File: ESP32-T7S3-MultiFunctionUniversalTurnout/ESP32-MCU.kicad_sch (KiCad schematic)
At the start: 7 parts, among them U201 TTGO-T7_S3-V1.1

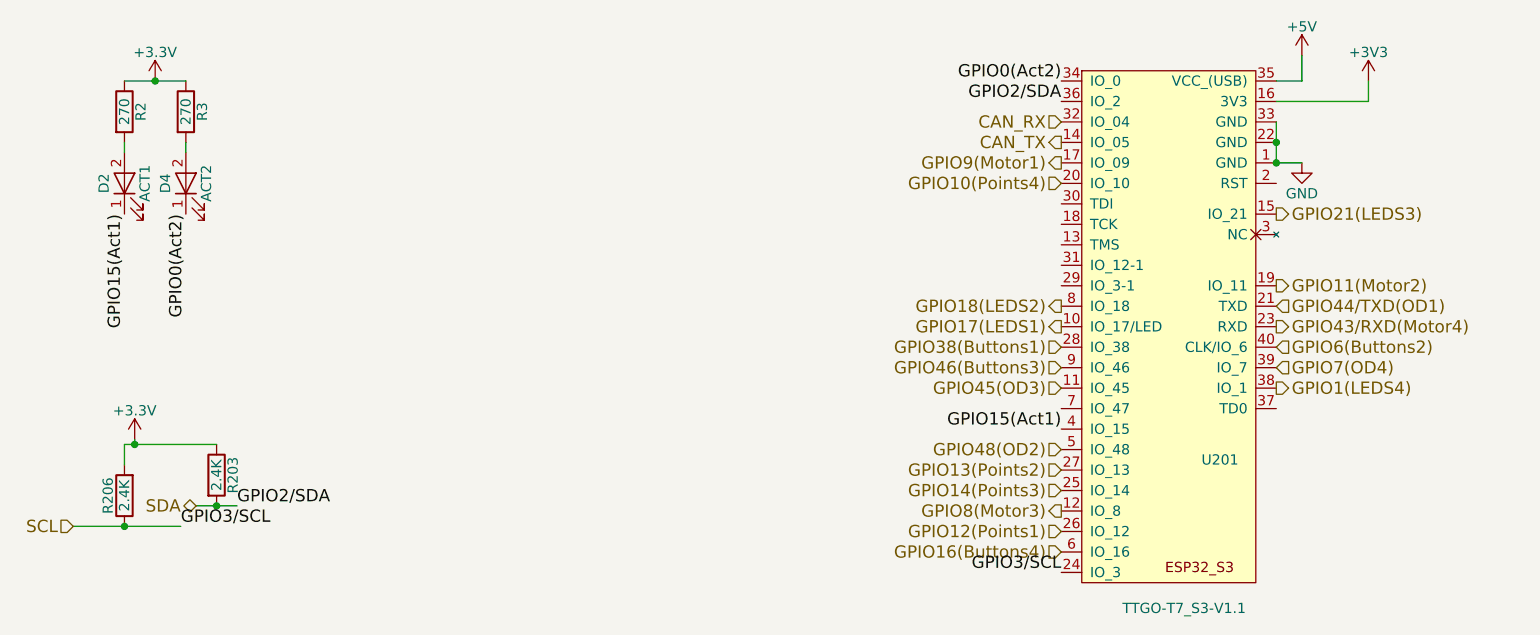
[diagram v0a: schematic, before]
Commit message: Change SDA from IO2 to IO40.
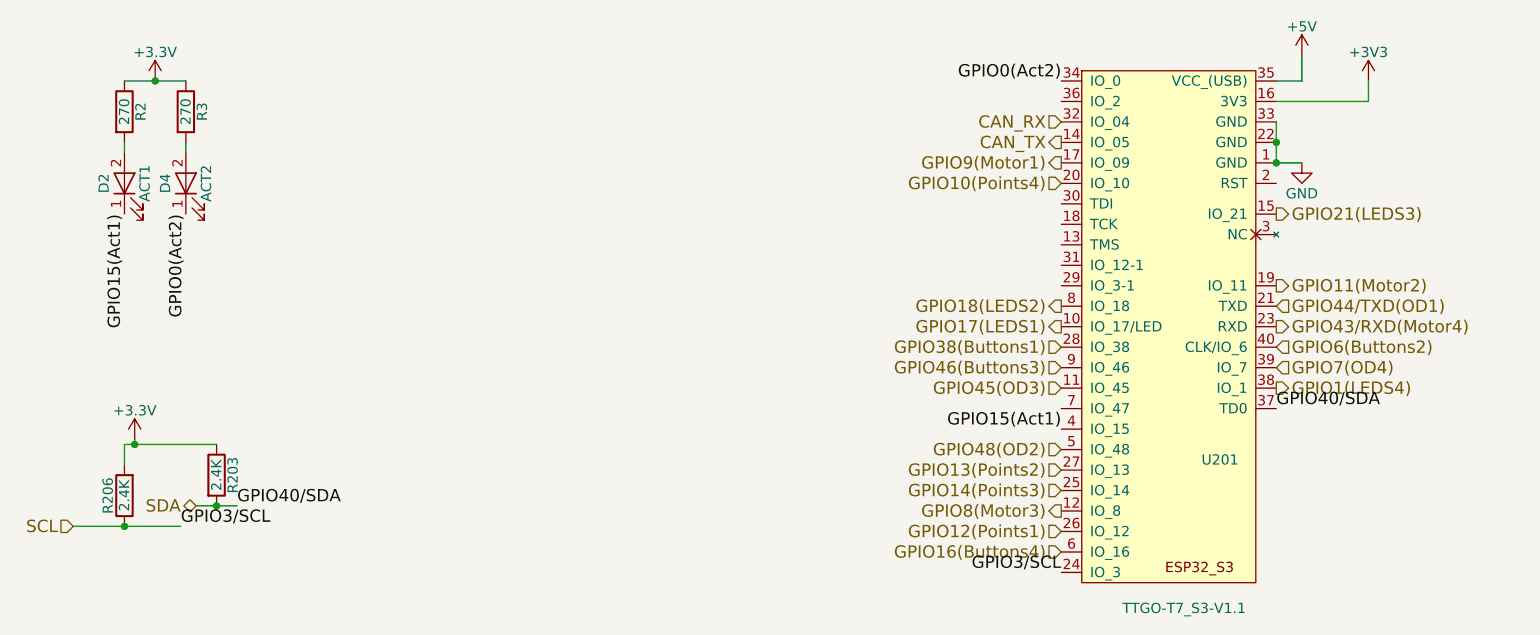
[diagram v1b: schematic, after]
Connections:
- net SDA: now also U201.37 (TD0); no longer U201.36 (IO_2)
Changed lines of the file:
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@@
     (effects (font (size 1.524 1.524)) (justify right bottom))
   )
-  (label "GPIO2/SDA" (at 213.995 66.04 180)
-    (effects (font (size 1.524 1.524)) (justify right bottom))
+  (label "GPIO40{slash}SDA" (at 240.665 104.14 0)
+    (effects (font (size 1.524 1.524)) (justify left bottom))
   )
   (label "GPIO3/SCL" (at 104.775 118.745 0)
@@
     (effects (font (size 1.524 1.524)) (justify right bottom))
   )
-  (label "GPIO2/SDA" (at 111.76 116.205 0)
+  (label "GPIO40{slash}SDA" (at 111.76 116.205 0)
     (effects (font (size 1.524 1.524)) (justify left bottom))
   )

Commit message: Reroute GPIOs using UART0 lines.
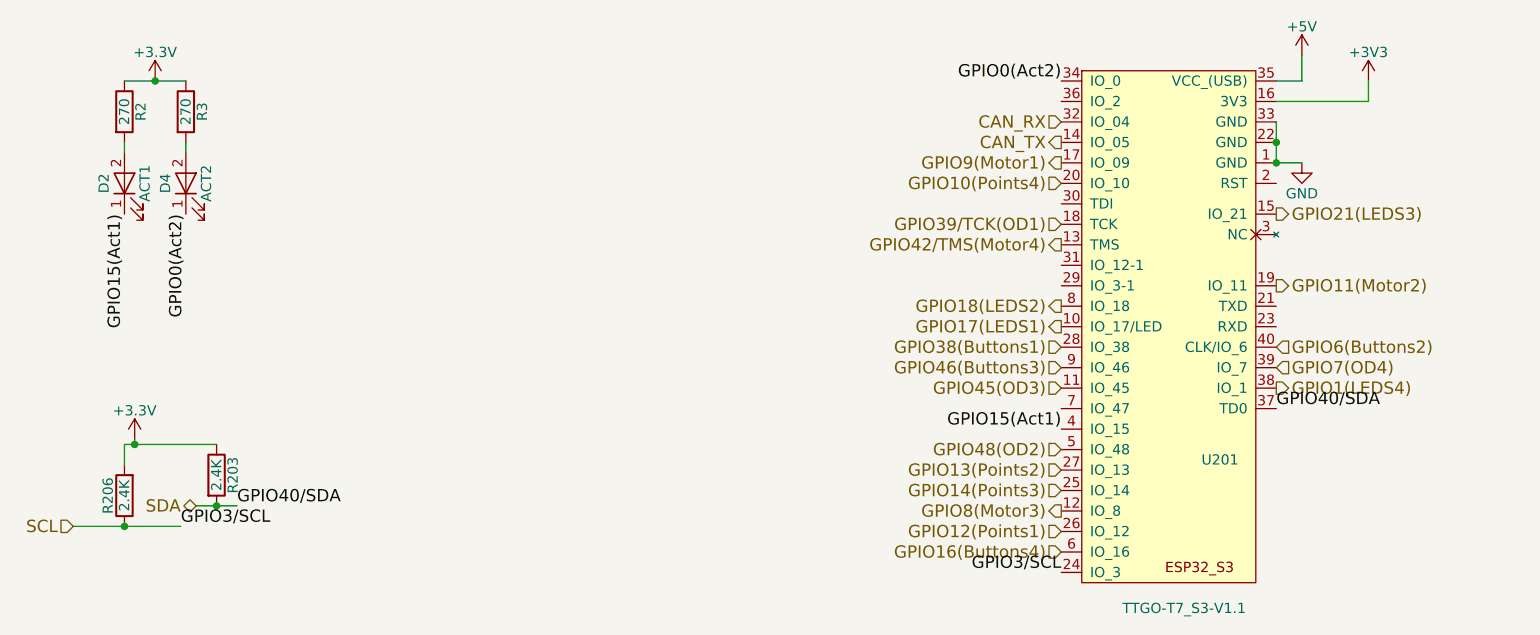
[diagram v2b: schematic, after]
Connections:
- net GPIO42/TMS(Motor4): now reaches U201.13 (TMS)
- net GPIO39/TCK(OD1): now reaches U201.18 (TCK)
- net GPIO43/RXD(Motor4): no longer names the net of U201.23 (RXD)
- net GPIO44/TXD(OD1): no longer names the net of U201.21 (TXD)
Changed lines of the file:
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@@
     (effects (font (size 1.524 1.524)) (justify left))
   )
-  (hierarchical_label "GPIO43/RXD(Motor4)" (shape output) (at 240.665 93.98 0)
-    (effects (font (size 1.524 1.524)) (justify left))
+  (hierarchical_label "GPIO42{slash}TMS(Motor4)" (shape output) (at 213.995 83.82 180)
+    (effects (font (size 1.524 1.524)) (justify right))
   )
-  (hierarchical_label "GPIO44/TXD(OD1)" (shape input) (at 240.665 91.44 0)
-    (effects (font (size 1.524 1.524)) (justify left))
+  (hierarchical_label "GPIO39{slash}TCK(OD1)" (shape input) (at 213.995 81.28 180)
+    (effects (font (size 1.524 1.524)) (justify right))
   )
   (hierarchical_label "GPIO8(Motor3)" (shape output) (at 213.995 116.84 180)
